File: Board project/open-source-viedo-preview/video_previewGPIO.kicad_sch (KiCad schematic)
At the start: 23 parts, among them J1 Conn_02x07_Odd_Even, J2 Conn_01x03, J3 Conn_01x03, J4 7499110124, J5 Micro_SD_Card_Det, J6 Conn_02x20_Odd_Even, U1 74LVC1G07, U2 74LVC1G07

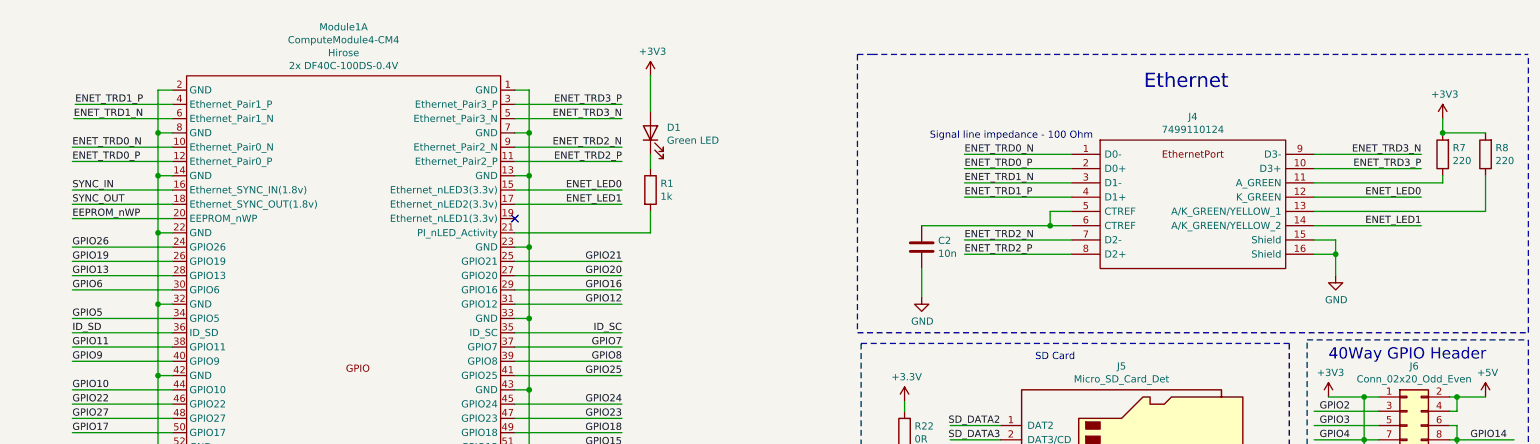
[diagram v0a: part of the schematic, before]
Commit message: added ESD protection on Ethernet lines and change net labels for this interface
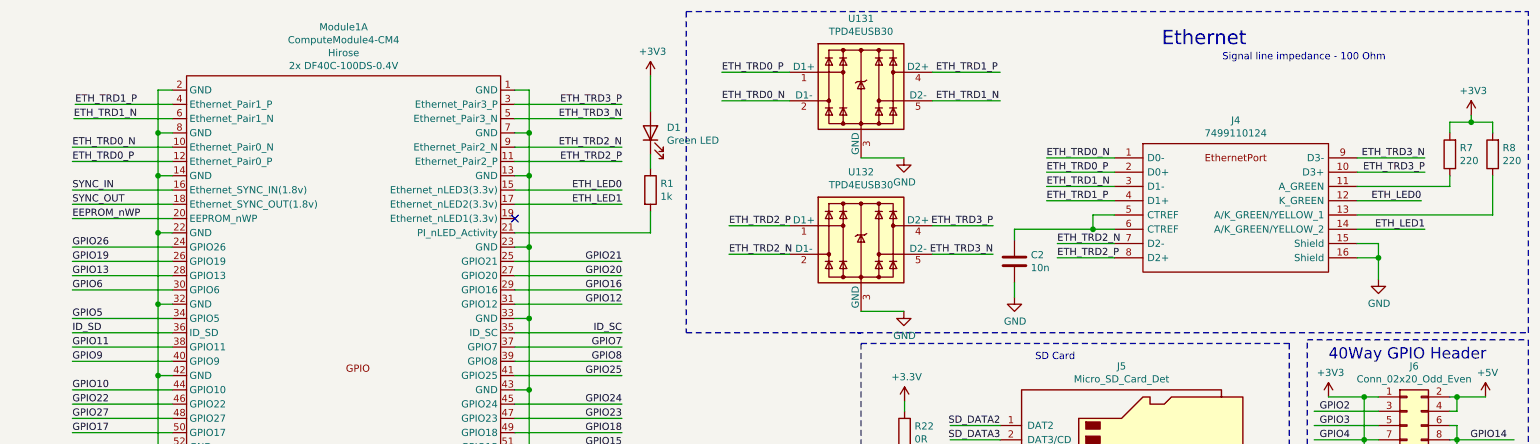
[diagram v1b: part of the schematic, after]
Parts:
- added U131, U132: TPD4EUSB30, Package_SON:USON-10_2.5x1.0mm_P0.5mm, symbol Power_Protection:TPD4EUSB30
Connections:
- net GND: now also U131.3 (GND), U131.8 (GND), U132.3 (GND), U132.8 (GND)
- net ENET_LED0 renamed ETH_LED0
- net ENET_LED1 renamed ETH_LED1
- net ENET_TRD0_N renamed ETH_TRD0_N
- net ETH_TRD0_N: now also U131.2 (D1-)
- net ENET_TRD0_P renamed ETH_TRD0_P
- net ETH_TRD0_P: now also U131.1 (D1+)
- net ENET_TRD1_N renamed ETH_TRD1_N
- net ETH_TRD1_N: now also U131.5 (D2-)
- net ENET_TRD1_P renamed ETH_TRD1_P
- net ETH_TRD1_P: now also U131.4 (D2+)
- net ENET_TRD2_N renamed ETH_TRD2_N
- net ETH_TRD2_N: now also U132.2 (D1-)
- net ENET_TRD2_P renamed ETH_TRD2_P
- net ETH_TRD2_P: now also U132.1 (D1+)
- net ENET_TRD3_N renamed ETH_TRD3_N
- net ETH_TRD3_N: now also U132.5 (D2-)
- net ENET_TRD3_P renamed ETH_TRD3_P
- net ETH_TRD3_P: now also U132.4 (D2+)
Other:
- moved on the sheet: C2, J4, R7, R8

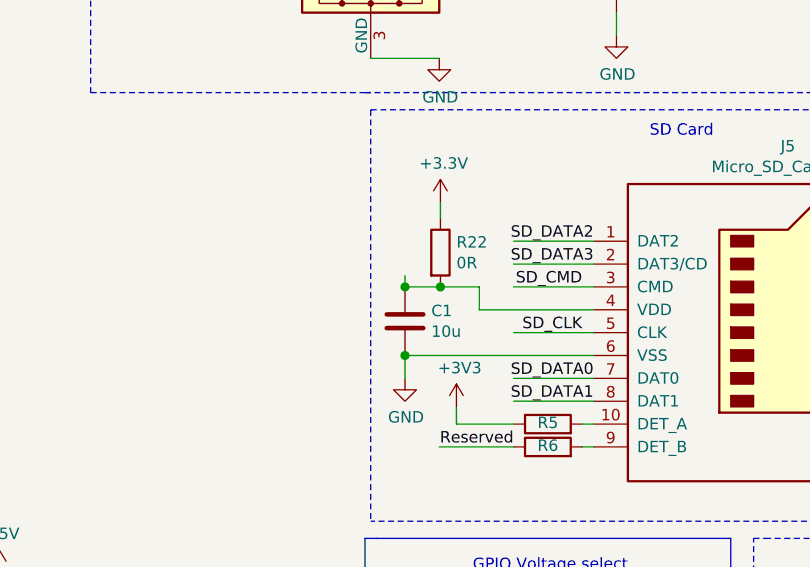
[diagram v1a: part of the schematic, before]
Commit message: Footprints added (without HDMI)
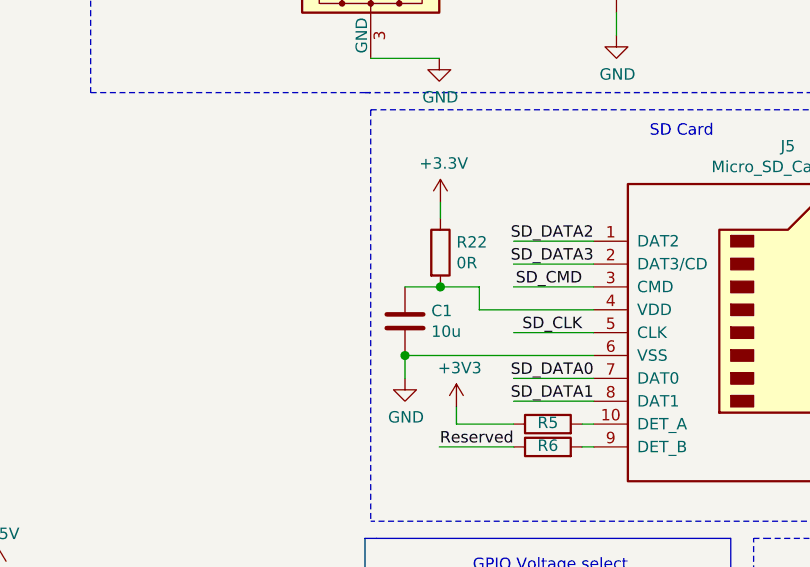
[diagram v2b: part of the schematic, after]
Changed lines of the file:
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@@
   (junction (at 102.87 116.84) (diameter 0.9144) (color 0 0 0 0))
   (junction (at 102.87 140.97) (diameter 0.9144) (color 0 0 0 0))
-  (junction (at 165.735 92.71) (diameter 1.016) (color 0 0 0 0))
   (junction (at 165.735 100.33) (diameter 1.016) (color 0 0 0 0))
   (junction (at 169.672 92.71) (diameter 1.016) (color 0 0 0 0))
@@
     (stroke (width 0) (type solid) (color 0 0 0 0))
   )
-  (wire (pts (xy 165.735 91.44) (xy 165.735 92.71))
-    (stroke (width 0) (type solid) (color 0 0 0 0))
-  )
